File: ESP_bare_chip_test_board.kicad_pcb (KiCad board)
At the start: 4 copper layers, 57.1 x 56.5 mm, 90 parts, among them J1101 Conn_01x04, J1201 NorComp - 112-024-113RYY1, J1301 Conn_01x06, J1302 Conn_01x06, J1303 Conn_01x10, J1501 Conn_01x04, J201 Conn_01x06, J501 Barrel_Jack, J502 PWR_IN, J503 ALTERNATE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

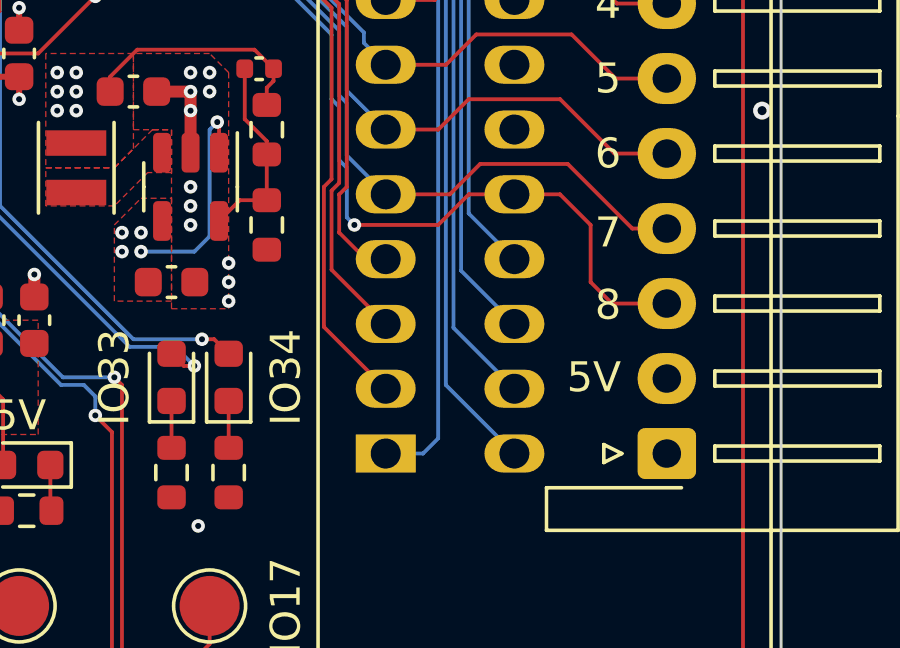
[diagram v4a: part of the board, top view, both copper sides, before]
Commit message: Add JLCPCB corrections for new components
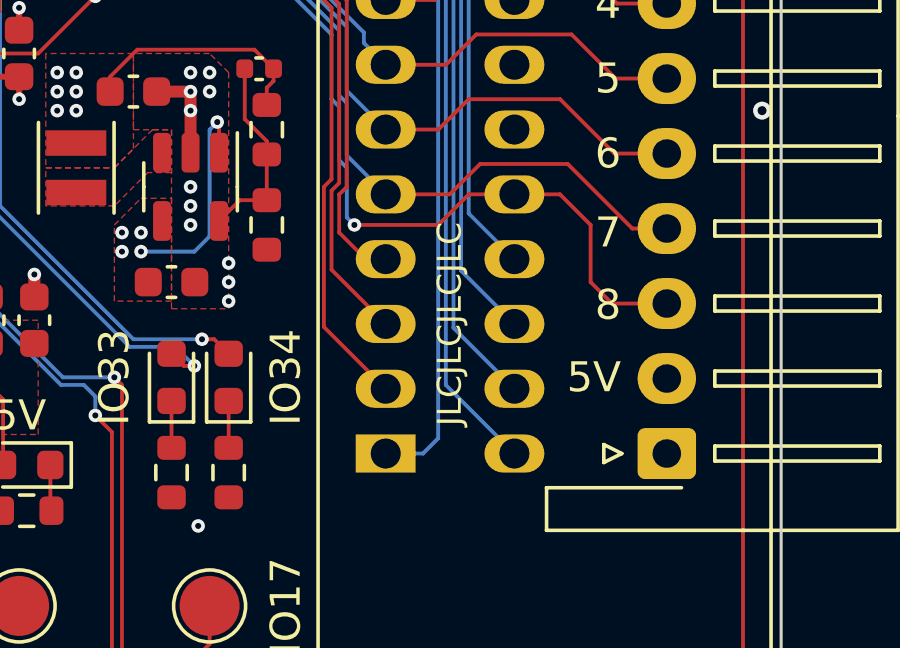
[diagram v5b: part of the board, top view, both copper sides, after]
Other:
- board text added: "JLCJLCJLCJLC"
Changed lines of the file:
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@@
 		(tags "LED")
 		(property "Reference" "D101"
-			(at 0 -1.43 270)
+			(at 0 -1.43 -90)
 			(layer "F.SilkS")
 			(hide yes)
@@
 		)
 		(property "Value" "YELLOW"
-			(at 0 1.43 270)
+			(at 0 1.43 -90)
 			(layer "F.Fab")
 			(effects
@@
 		)
 		(fp_text user "${REFERENCE}"
-			(at 0 0 270)
+			(at 0 0 -90)
 			(layer "F.Fab")
 			(effects
@@
 		(tags "LED")
 		(property "Reference" "D102"
-			(at 0 -1.43 270)
+			(at 0 -1.43 -90)
 			(layer "F.SilkS")
 			(hide yes)
@@
 		)
 		(property "Value" "YELLOW"
-			(at 0 1.43 270)
+			(at 0 1.43 -90)
 			(layer "F.Fab")
 			(effects
@@
 		)
 		(fp_text user "${REFERENCE}"
-			(at 0 0 270)
+			(at 0 0 -90)
 			(layer "F.Fab")
 			(effects
@@
 		)
 	)
+	(gr_text "JLCJLCJLCJLC"
+		(at 160.401 89.662 90)
+		(layer "F.SilkS")
+		(effects
+			(font
+				(size 0.8 0.8)
+				(thickness 0.15)
+			)
+		)
+	)

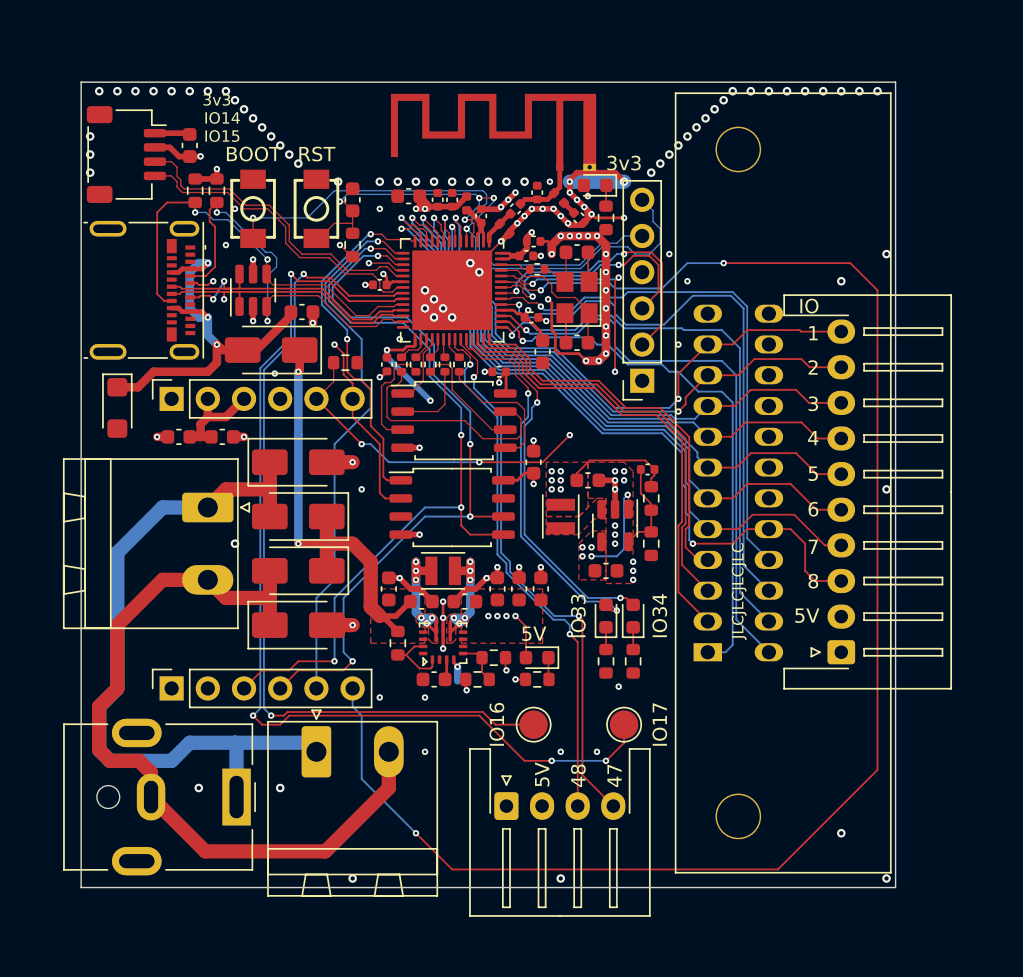
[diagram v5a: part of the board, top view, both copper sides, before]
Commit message: Silkscreen work. Edit tittle block/version number
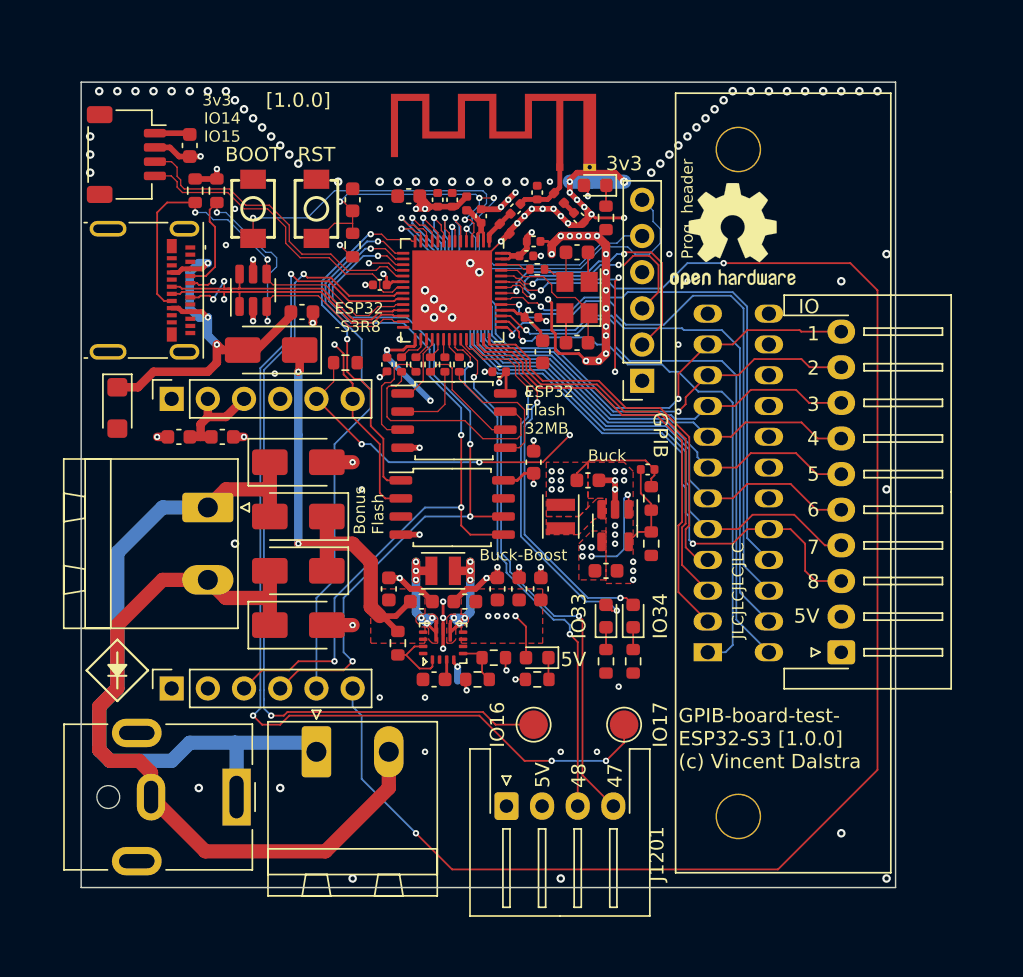
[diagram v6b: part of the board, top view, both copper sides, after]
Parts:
- added REF**: OSHW-Logo2_9.8x8mm_SilkScreen, Symbol:OSHW-Logo2_9.8x8mm_SilkScreen, F.Cu at (160.0, 64.8)
- added REF**: OSHW-Logo2_9.8x8mm_SilkScreen, Symbol:OSHW-Logo2_9.8x8mm_SilkScreen, B.Cu at (160.0, 64.8)
- R1301: value 1.5k -> 1.5kΩ
- R601, R602: value 5.1k -> 5.1kΩ
- U302: value ESP32-S3 -> ESP32-S3R8
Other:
- board text added: "All power inputs are rectified"
- board text added: "Bonus Flash"
- board text added: "Buck"
- board text added: "Buck-Boost"
- board text added: "ESP32 -S3R8"
- board text added: "ESP32 Flash 32MB"
- board text added: "GPIB"
- board text added: "GPIB-board-test- ESP32-S3 [1.0.0] (c) Vincent Dalstra"
- board text added: "Prog. header"
- board text added: "USB-prog Power-in only"
- board text added: "USR-ES1 Ethernet Cable dir:"
- board text added: "V_{IN} 3-17V"
- board text added: "[${REVISION}]"

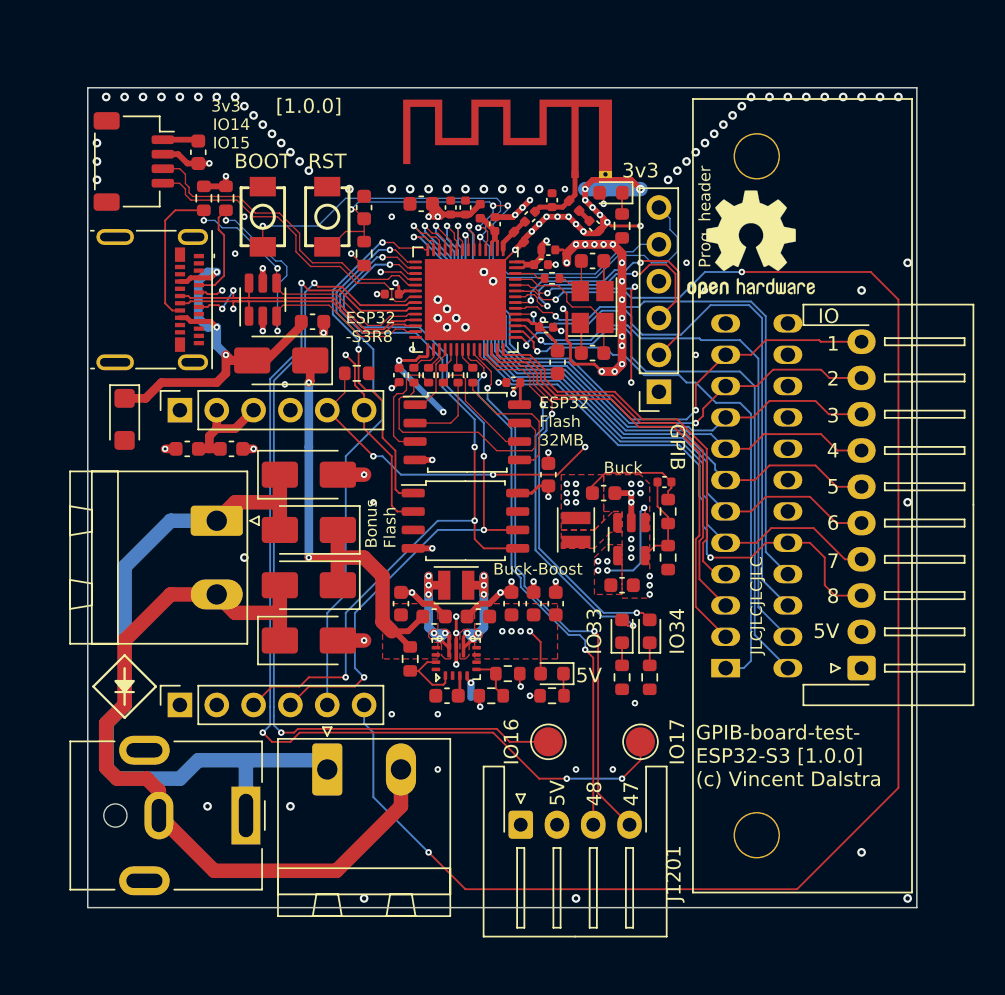
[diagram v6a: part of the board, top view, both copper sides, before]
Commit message: Final corrections and silkscreen labels
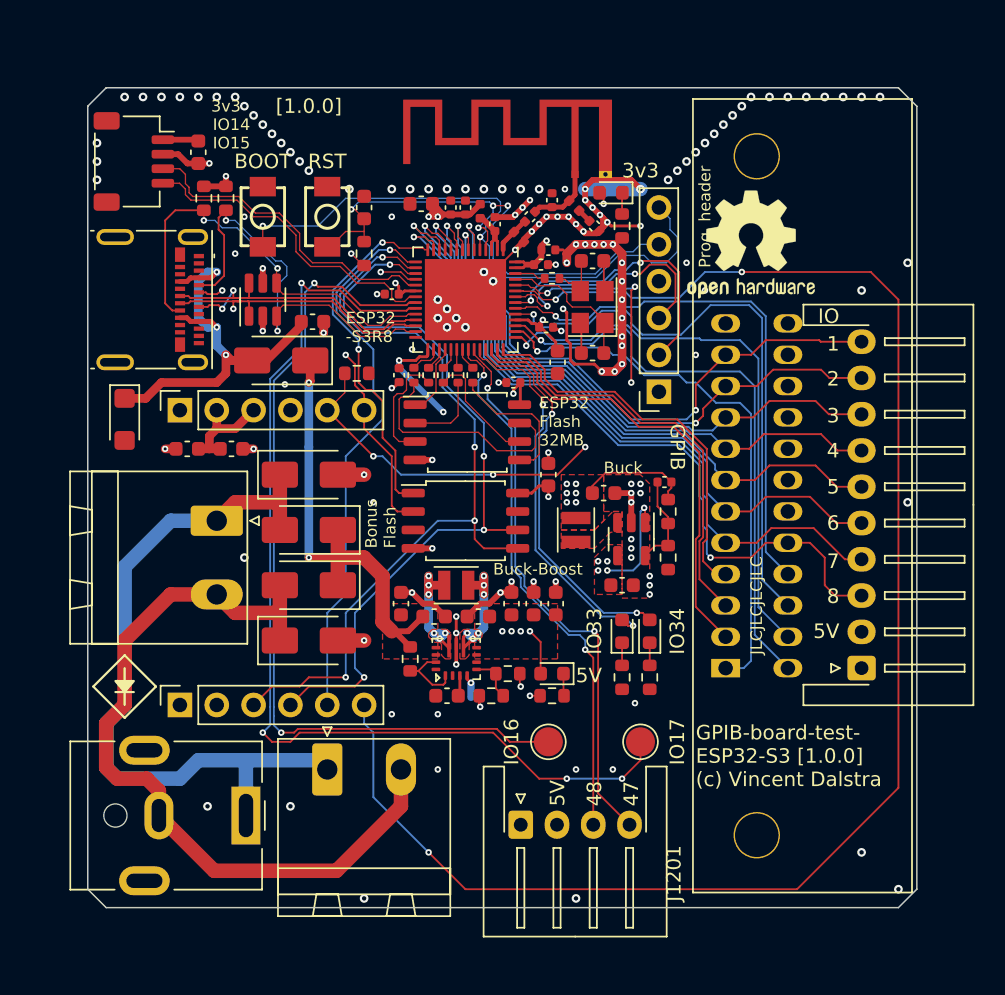
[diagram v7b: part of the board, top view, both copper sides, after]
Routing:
- net GND: vias 151 -> 149
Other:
- outline, holes or cut-outs redrawn
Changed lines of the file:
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@@
 	)
 	(gr_line
-		(start 171.45 110.49)
-		(end 114.3 110.49)
+		(start 170.18 110.49)
+		(end 115.57 110.49)
 		(stroke
 			(width 0.1)
@@
 	)
 	(gr_line
-		(start 114.3 53.975)
-		(end 171.45 53.975)
+		(start 115.57 110.49)
+		(end 114.3 109.22)
 		(stroke
 			(width 0.1)
@@
 	)
 	(gr_line
-		(start 171.45 53.975)
-		(end 171.45 110.49)
+		(start 170.18 110.49)
+		(end 171.45 109.22)
 		(stroke
 			(width 0.1)
@@
 	)
 	(gr_line
-		(start 114.3 110.49)
-		(end 114.3 53.975)
+		(start 114.3 55.245)
+		(end 115.57 53.975)
 		(stroke
 			(width 0.1)
@@
 		(layer "Edge.Cuts")
 	)
+	(gr_line
+		(start 115.57 53.975)
+		(end 170.18 53.975)
+		(stroke
+			(width 0.1)
+			(type default)
+		)
+		(layer "Edge.Cuts")
+	)
+	(gr_line
+		(start 171.45 55.245)
+		(end 171.45 109.22)
+		(stroke
+			(width 0.1)
+			(type default)
+		)
+		(layer "Edge.Cuts")
+	)
+	(gr_line
+		(start 170.18 53.975)
+		(end 171.45 55.245)
+		(stroke
+			(width 0.1)
+			(type default)
+		)
+		(layer "Edge.Cuts")
+	)
+	(gr_line
+		(start 114.3 109.22)
+		(end 114.3 55.245)
+		(stroke
+			(width 0.1)
+			(type default)
+		)
+		(layer "Edge.Cuts")
+	)
 	(gr_text "USR-ES1\nEthernet\nCable dir:"
 		(at 133.35 78.105 0)
@@
 	)
 	(via
-		(at 170.815 109.855)
+		(at 170.18 109.22)
 		(size 0.6)
 		(drill 0.3)
@@
 	)
 	(via
-		(at 115.57 54.61)
-		(size 0.6)
-		(drill 0.3)
-		(layers "F.Cu" "B.Cu")
-		(free yes)
-		(net 2)
-	)
-	(via
 		(at 136.525 60.96)
 		(size 0.6)
@@
 		(size 0.6)
 		(drill 0.3)
-		(layers "F.Cu" "B.Cu")
-		(free yes)
-		(net 2)
-	)
-	(via
-		(at 170.18 54.61)
-		(size 0.6)
-		(drill 0.3)
